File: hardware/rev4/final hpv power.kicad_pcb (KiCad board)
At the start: 2 copper layers, 69.5 x 54 mm, 27 parts, among them J1 Conn_02x03_Odd_Even, J2 Conn_01x04_Pin, Q1 PNP, U1 ESP32-S3-MINI-1, U2 MCP1825S, U3 HX711

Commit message: fixed up things for justin to look
fixed up things for justin to look
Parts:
- removed J1: Conn_02x03_Odd_Even, Connector_IDC:IDC-Header_2x03_P2.54mm_Vertical
- added J3: USB_C_Receptacle_USB2.0_14P, Connector_USB:USB_C_Receptacle_GCT_USB4110, F.Cu at (105.9, 102.3)
- added R7: 5.1k, Resistor_SMD:R_0805_2012Metric, F.Cu at (113.8, 99.1)
- added R8: 5.1k, Resistor_SMD:R_0805_2012Metric, F.Cu at (113.4, 106.0)
- C1, C10, C11, C12, C2, C3, C4, C5, C6, C7, C8, C9: footprint Capacitor_SMD:C_0603_1608Metric -> Capacitor_SMD:C_0805_2012Metric
- D1, D2: footprint LED_SMD:LED_0603_1608Metric -> LED_SMD:LED_0805_2012Metric
- R1, R2, R3, R4, R5, R6: footprint Resistor_SMD:R_0603_1608Metric -> Resistor_SMD:R_0805_2012Metric
- moved C3 6.66 mm to (130.6, 114.8)
- moved C2 6.61 mm to (127.5, 114.8)
- moved C5 6.53 mm to (121.2, 107.3)
- moved C7 6.53 mm to (121.2, 110.8)
- moved U2 6.53 mm to (127.8, 109.3)
- moved C1 6.50 mm to (124.4, 114.9)
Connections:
- net BATT renamed VBUS
- U1 pad 23: unconnected-(U1-USB_D--Pad23) -> /D-
- U1 pad 24: unconnected-(U1-USB_D+-Pad24) -> /D+
- U1 pad 39: /TX -> unconnected-(U1-TXD0-Pad39)
- U1 pad 40: /RX -> unconnected-(U1-RXD0-Pad40)
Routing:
- net VBUS: track 2.78 -> 39.5 mm
- net /D+: track 0.00 -> 30.2 mm, vias 0 -> 2
- net /D-: track 0.00 -> 30.1 mm, vias 0 -> 2
- net GND: track 115.0 -> 130.4 mm, vias 37 -> 45
- net /TX: track 11.0 -> 0.00 mm
- net /RX: track 10.3 -> 0.00 mm
- net Net-(J3-CC1): track 0.00 -> 4.10 mm
- net Net-(J3-CC2): track 0.00 -> 3.73 mm
- net +3.3V: track 23.3 -> 26.9 mm

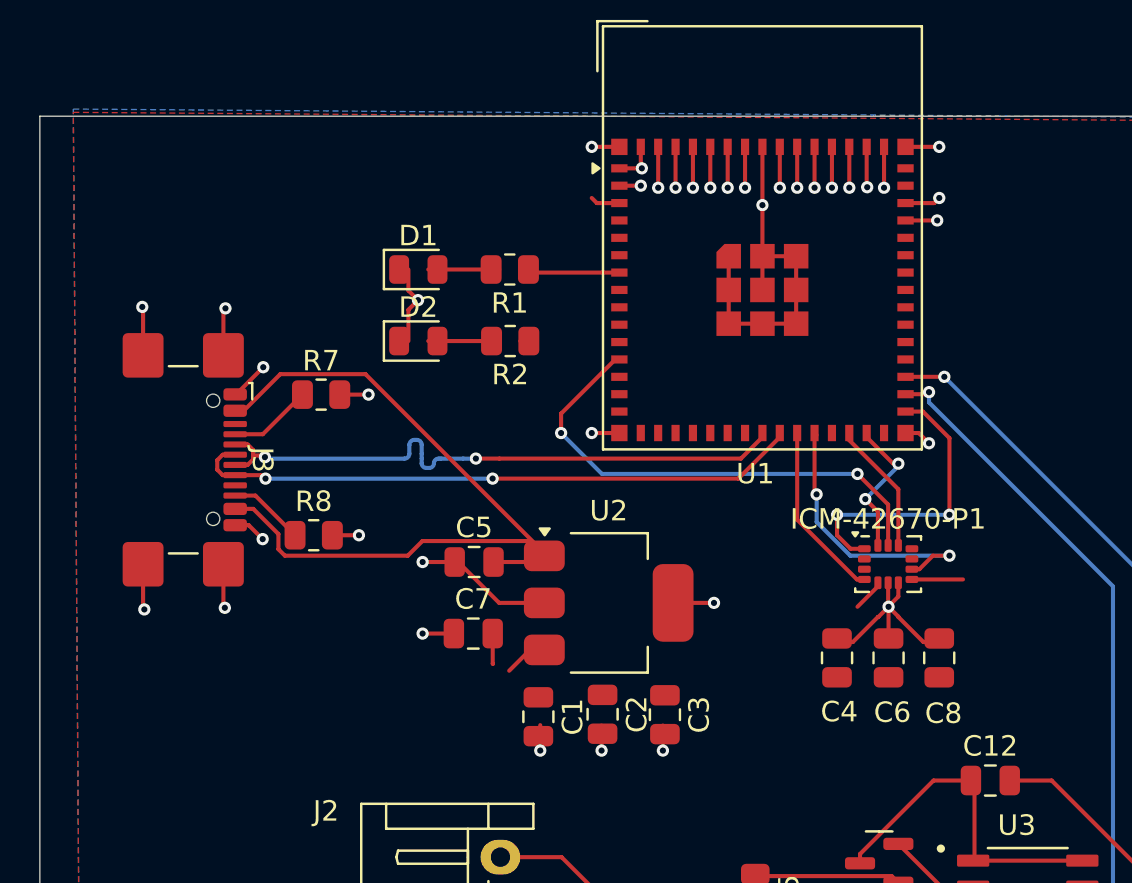
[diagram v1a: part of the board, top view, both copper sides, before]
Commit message: Update final hpv power.kicad_pcb
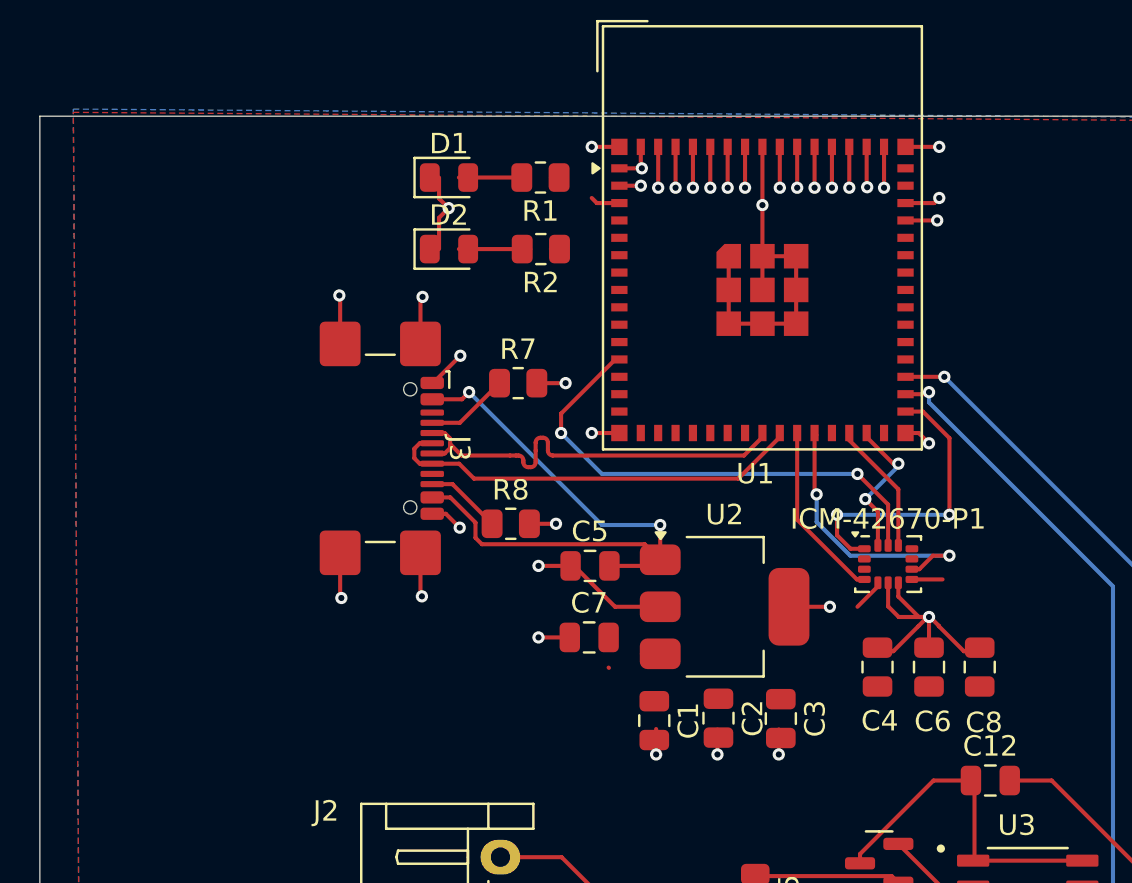
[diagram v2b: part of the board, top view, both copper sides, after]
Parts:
- moved R8 9.66 mm to (123.0, 105.4)
- moved J3 9.66 mm to (115.5, 101.8)
- moved R7 9.66 mm to (123.4, 98.6)
- moved C1 5.67 mm to (130.1, 115.1)
- moved C5 5.67 mm to (126.9, 107.5)
- moved C7 5.67 mm to (126.9, 111.0)
- moved U2 5.67 mm to (133.5, 109.5)
- moved C2 5.67 mm to (133.2, 115.0)
- moved C3 5.67 mm to (136.2, 115.0)
- moved D1 4.74 mm to (120.0, 88.5)
- moved D2 4.74 mm to (120.0, 92.0)
- moved R1 4.74 mm to (124.5, 88.5)
- moved R2 4.74 mm to (124.5, 92.0)
- moved C4 2.03 mm to (141.0, 112.5)
- moved C6 2.03 mm to (143.5, 112.5)
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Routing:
- net /D-: track 30.1 -> 20.7 mm, vias 2 -> 0
- net /D+: track 30.2 -> 20.8 mm, vias 2 -> 0
- net VBUS: track 39.5 -> 31.9 mm, vias 0 -> 2
- net /LED: track 4.91 -> 0.71 mm
- net +3.3V: track 26.9 -> 23.0 mm
- net GND: track 130.4 -> 133.5 mm

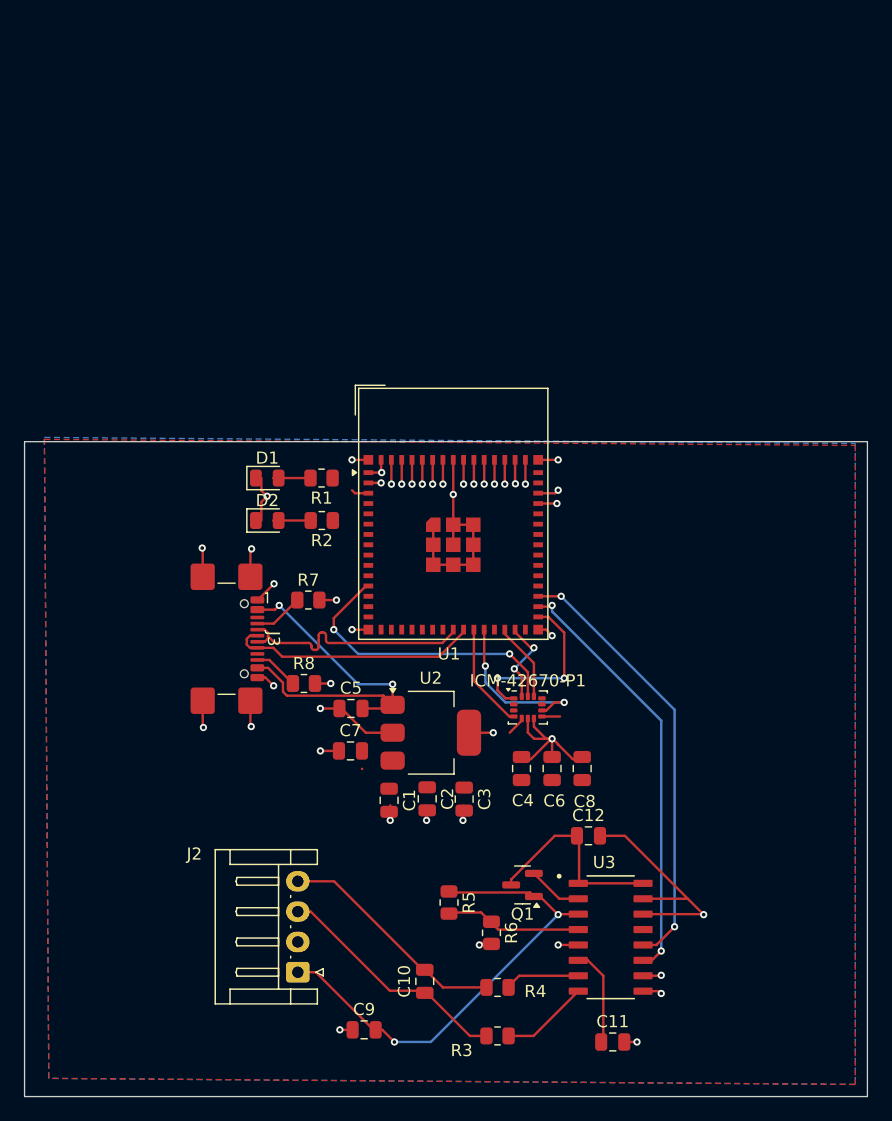
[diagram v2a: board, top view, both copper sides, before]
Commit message: Updated PCB and schematic for esp32 s3 wroom
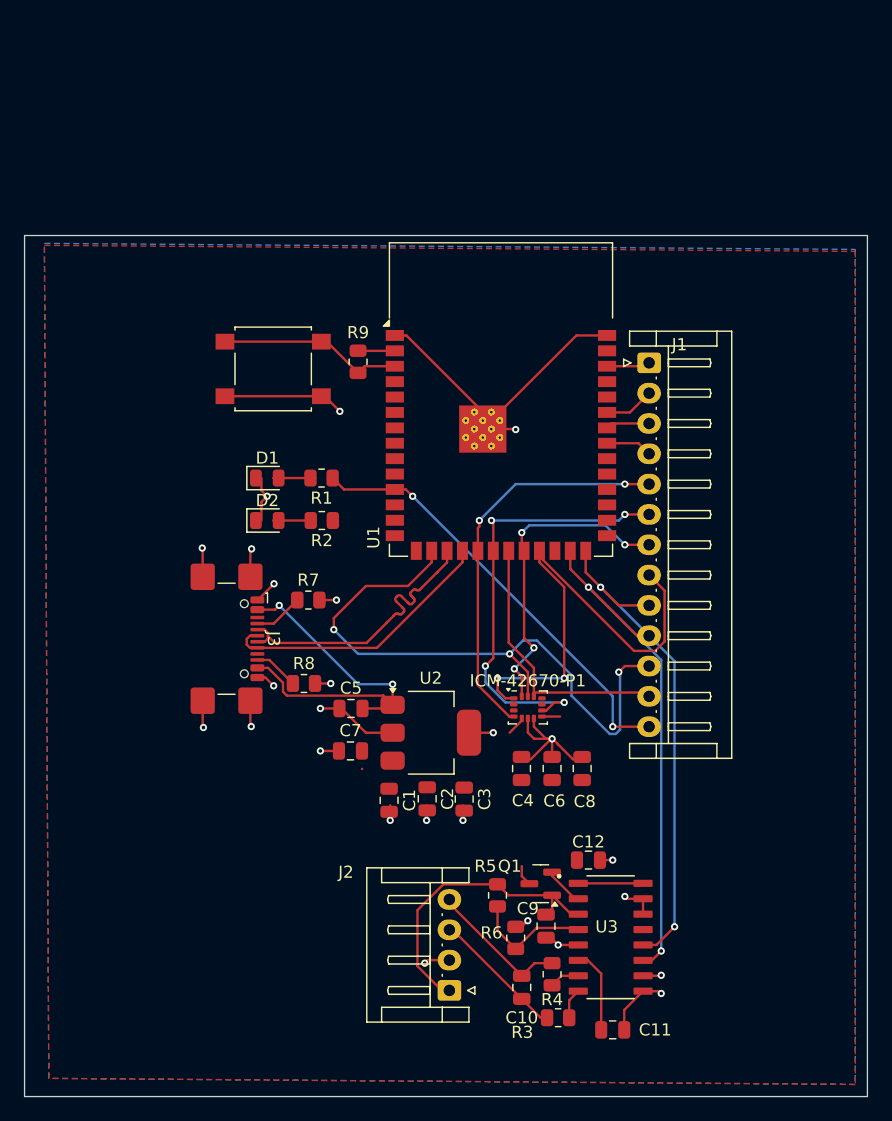
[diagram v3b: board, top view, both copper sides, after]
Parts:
- added J1: Conn_01x13_Pin, Connector_JST:JST_EH_S13B-EH_1x13_P2.50mm_Horizontal, F.Cu at (151.5, 79.0)
- added R9: 5.1k, Resistor_SMD:R_0805_2012Metric, F.Cu at (127.5, 78.9)
- added SW2: SW_SPST, Button_Switch_SMD:SW_SPST_B3S-1000, F.Cu at (120.5, 79.5)
- U1: value ESP32-S3-MINI-1 -> ESP32-S3-WROOM-1; footprint RF_Module:ESP32-S2-MINI-1 -> RF_Module:ESP32-S3-WROOM-1
- moved C9 17.3 mm to (143.0, 125.5), turned to 90 degrees
- moved J2 12.6 mm to (135.0, 130.8)
- moved U1 10.2 mm to (139.3, 82.0)
- moved C10 8.02 mm to (141.0, 130.5)
- moved R3 5.22 mm to (144.0, 133.0)
- moved R4 4.63 mm to (143.5, 129.4), turned to 90 degrees
- moved R5 4.04 mm to (139.0, 122.9)
- moved R6 2.04 mm to (140.5, 126.4)
- moved C12 2.00 mm to (146.5, 120.0)
- moved Q1 1.50 mm to (142.6, 122.0)
- moved C11 1.00 mm to (148.5, 134.0)
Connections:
- R6 pad 1: Net-(U3-VFB) -> GND
- R6 pad 2: GND -> Net-(U3-VFB)
- U1 pad 11: unconnected-(U1-IO7-Pad11) -> /LED
- U1 pad 12: /SCLK -> unconnected-(U1-IO8-Pad12)
- U1 pad 16: unconnected-(U1-IO12-Pad16) -> /SCLK
- U1 pad 17: unconnected-(U1-IO13-Pad17) -> /D-
- U1 pad 18: unconnected-(U1-IO14-Pad18) -> /D+
- U1 pad 19: unconnected-(U1-IO15-Pad19) -> /INT1 Gyro
- U1 pad 2: GND -> +3.3V
- U1 pad 20: unconnected-(U1-IO16-Pad20) -> /INT2 Gyro
- U1 pad 21: unconnected-(U1-IO17-Pad21) -> /CS Gyro
- U1 pad 22: unconnected-(U1-IO18-Pad22) -> /MOSI
- U1 pad 23: /D- -> /MISO
- U1 pad 24: /D+ -> unconnected-(U1-IO47-Pad24)
- U1 pad 25: /INT1 Gyro -> /HX711 PDSCK
- U1 pad 26: /INT2 Gyro -> /HX711 DOUT
- U1 pad 28: /CS Gyro -> unconnected-(U1-IO35-Pad28)
- U1 pad 29: /MOSI -> unconnected-(U1-IO36-Pad29)
- U1 pad 3: +3.3V -> Net-(SW2-A)
- U1 pad 31: /MISO -> unconnected-(U1-IO38-Pad31)
- U1 pad 32: /HX711 PDSCK -> unconnected-(U1-IO39-Pad32)
- U1 pad 33: /HX711 DOUT -> /GPIO12
- U1 pad 34: unconnected-(U1-IO38-Pad34) -> /GPIO11
- U1 pad 35: unconnected-(U1-IO39-Pad35) -> /GPIO10
- U1 pad 38: unconnected-(U1-IO42-Pad38) -> /GPIO9
- U1 pad 40: unconnected-(U1-RXD0-Pad40) -> GND
- U1 pad 41: unconnected-(U1-IO45-Pad41) -> GND
- U1 pad 7: /LED -> unconnected-(U1-IO7-Pad7)
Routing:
- net /LED: track 0.71 -> 36.8 mm, vias 0 -> 2
- net GND: track 133.5 -> 101.9 mm, vias 45 -> 25
- net /SCLK: track 24.3 -> 52.7 mm, vias 2 -> 3
- net /MISO: track 14.6 -> 39.8 mm
- net /INT1 Gyro: track 8.74 -> 32.9 mm, vias 0 -> 2
- net /INT2 Gyro: track 14.0 -> 36.5 mm, vias 2 -> 4
- net /MOSI: track 7.21 -> 26.2 mm, vias 2 -> 4
- net /CS Gyro: track 6.49 -> 22.8 mm
- net Net-(SW2-A): track 0.00 -> 15.3 mm
- net Net-(J2-Pin_1): track 39.6 -> 25.1 mm, vias 2 -> 0
- net /HX711 PDSCK: track 35.2 -> 44.6 mm
- net Net-(J2-Pin_3): track 19.9 -> 11.1 mm
- net +3.3V: track 23.0 -> 14.9 mm
- net Net-(J2-Pin_4): track 19.3 -> 11.7 mm
- net /HX711 DOUT: track 36.2 -> 41.9 mm
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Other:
- board size 69.5 x 54 mm -> 69.5 x 71 mm

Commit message: Rewired the HX711 on pcb and shrunk pcb size
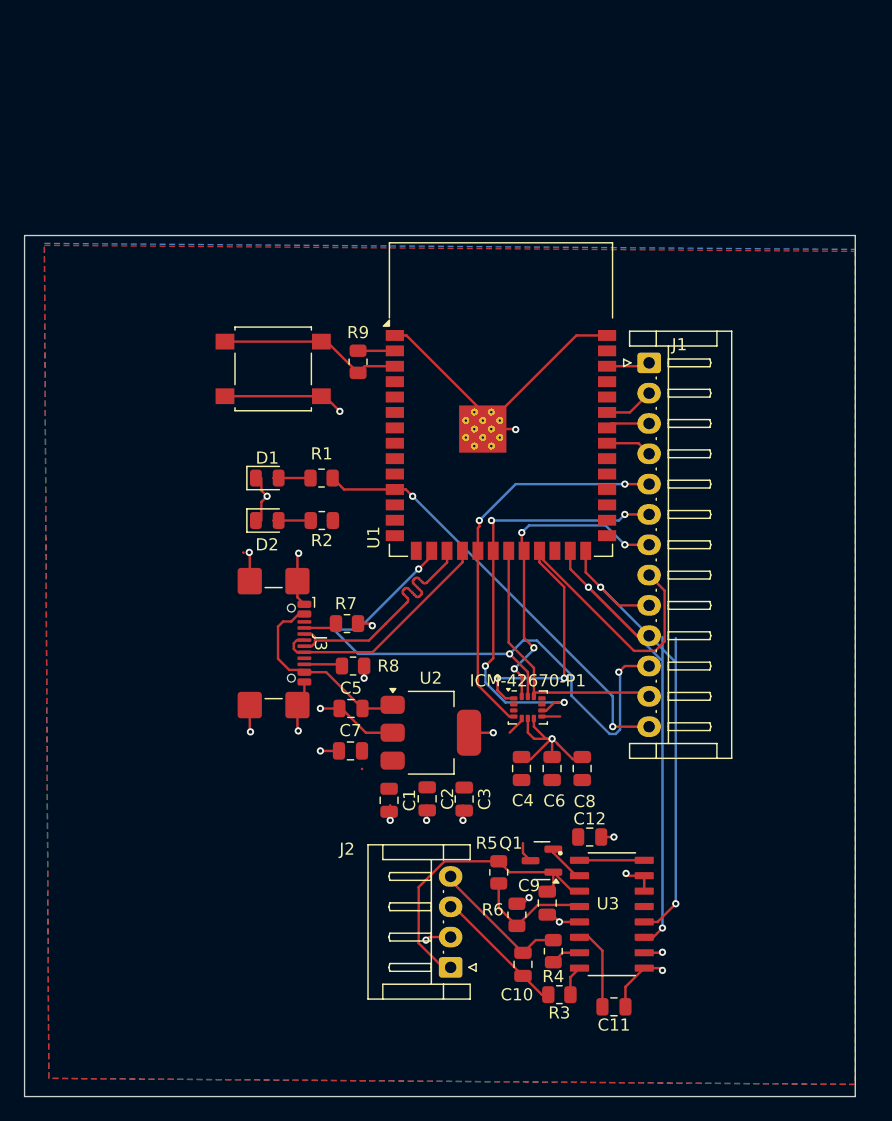
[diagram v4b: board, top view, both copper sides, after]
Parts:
- moved R8 4.30 mm to (127.1, 104.0)
- moved J3 3.90 mm to (119.4, 102.1)
- moved R7 3.73 mm to (126.6, 100.5)
- moved C10 1.90 mm to (141.1, 128.6)
- moved C11 1.90 mm to (148.6, 132.1)
- moved C12 1.90 mm to (146.6, 118.1)
- moved C9 1.90 mm to (143.1, 123.5)
- moved J2 1.90 mm to (135.1, 128.8)
- moved Q1 1.90 mm to (142.7, 120.0)
- moved R3 1.90 mm to (144.1, 131.1)
- moved R4 1.90 mm to (143.6, 127.5)
- moved R5 1.90 mm to (139.1, 121.0)
- moved R6 1.90 mm to (140.6, 124.5)
- moved U3 1.90 mm to (148.4, 124.5)
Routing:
- net VBUS: track 31.9 -> 16.8 mm, vias 2 -> 0
- net /D+: track 23.2 -> 19.5 mm
- net /D-: track 24.3 -> 20.6 mm
- net Net-(J3-CC1): track 4.10 -> 2.75 mm
- net Net-(J3-CC2): track 3.73 -> 3.16 mm
- net GND: track 101.9 -> 102.4 mm, vias 25 -> 23
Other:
- board size 69.5 x 71 mm -> 68.5 x 71 mm

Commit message: Fixing up PCB
added pull up resistor, replaced esp footprint, added header
made are a lot smaller
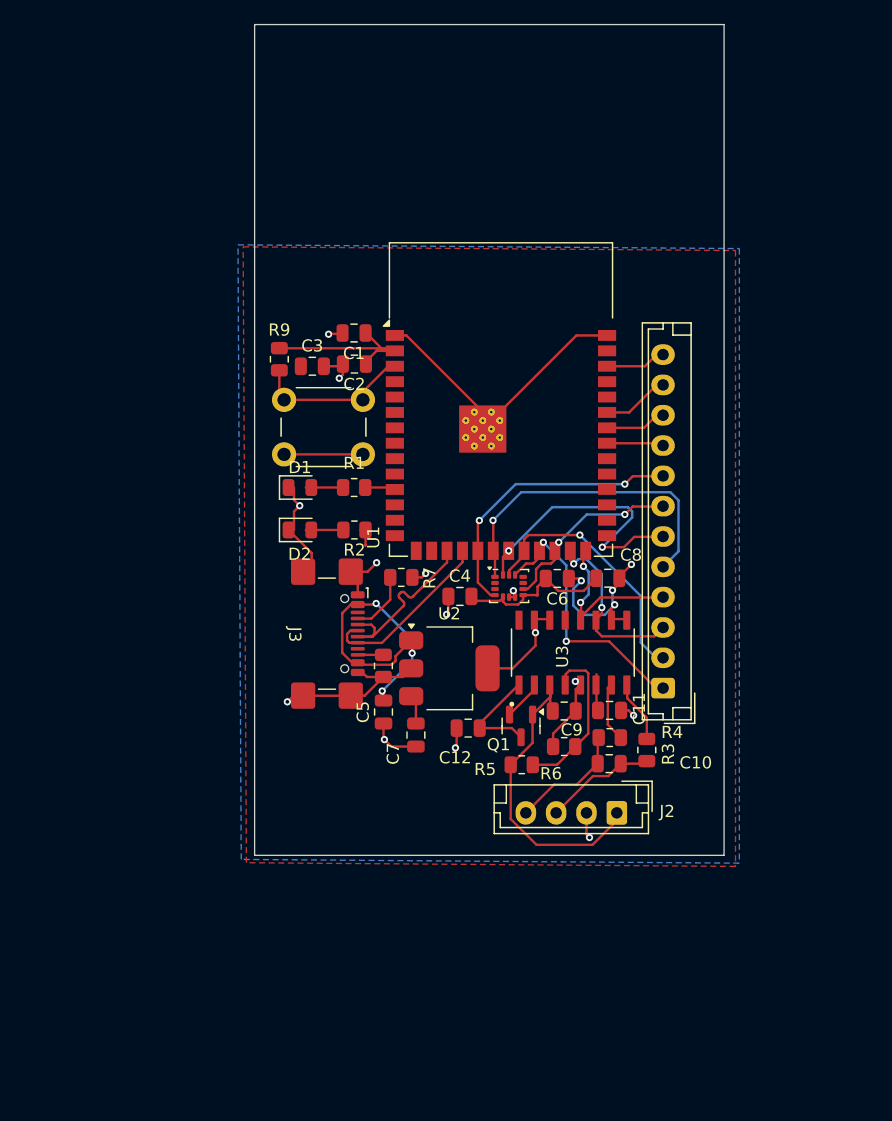
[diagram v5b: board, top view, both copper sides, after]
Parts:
- J1: value Conn_01x13_Pin -> Conn_01x12; footprint Connector_JST:JST_EH_S13B-EH_1x13_P2.50mm_Horizontal -> Connector_JST:JST_EH_B12B-EH-A_1x12_P2.50mm_Vertical
- J2: footprint Connector_JST:JST_EH_S4B-EH_1x04_P2.50mm_Horizontal -> Connector_JST:JST_EH_B4B-EH-A_1x04_P2.50mm_Vertical
- SW2: footprint Button_Switch_SMD:SW_SPST_B3S-1000 -> Button_Switch_THT:SW_PUSH_6mm_H4.3mm
- moved C1 38.6 mm to (127.2, 76.5), turned to 180 degrees
- moved C3 37.8 mm to (123.7, 79.3), turned to 0 degrees
- moved C2 36.3 mm to (127.2, 79.1), turned to 180 degrees
- moved J1 26.8 mm to (152.7, 105.8), turned to 90 degrees
- moved C11 24.4 mm to (148.2, 107.7)
- moved U3 21.8 mm to (145.2, 102.9), turned to 90 degrees
- moved R3 21.4 mm to (151.3, 110.9), turned to 90 degrees
- moved J2 18.7 mm to (148.8, 116.1), turned to 180 degrees
- moved R4 18.2 mm to (148.3, 109.9), turned to 180 degrees
- moved C10 18.0 mm to (148.2, 112.0), turned to 180 degrees
- moved C9 15.9 mm to (144.5, 107.7), turned to 180 degrees
- moved C8 15.8 mm to (148.1, 96.8), turned to 180 degrees
- moved C6 15.7 mm to (143.9, 96.8), turned to 180 degrees
- moved C4 15.1 mm to (135.9, 98.3), turned to 0 degrees
- moved R6 14.4 mm to (144.5, 110.6), turned to 0 degrees
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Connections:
- J1 pad 1: /GPIO9 -> /CS Gyro
- J1 pad 10: /HX711 PDSCK -> /GPIO11
- J1 pad 11: /SCLK -> /GPIO10
- J1 pad 12: /CS Gyro -> /GPIO9
- J1 pad 2: /GPIO10 -> /SCLK
- J1 pad 3: /GPIO11 -> /HX711 PDSCK
- J1 pad 4: /GPIO12 -> /HX711 DOUT
- J1 pad 5: /INT1 Gyro -> /MISO
- J1 pad 6: /INT2 Gyro -> /MOSI
- J1 pad 7: /MOSI -> /INT2 Gyro
- J1 pad 8: /MISO -> /INT1 Gyro
- J1 pad 9: /HX711 DOUT -> /GPIO12
- U1 pad 16: /SCLK -> unconnected-(U1-IO46-Pad16)
- U1 pad 20: /INT2 Gyro -> /MISO
- U1 pad 21: /CS Gyro -> /MOSI
- U1 pad 22: /MOSI -> /SCLK
- U1 pad 23: /MISO -> /CS Gyro
- U1 pad 24: unconnected-(U1-IO47-Pad24) -> /INT2 Gyro
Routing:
- net /LED: track 36.8 -> 3.22 mm, vias 2 -> 0
- net /SCLK: track 52.3 -> 21.8 mm, vias 3 -> 1
- net /HX711 PDSCK: track 44.6 -> 15.7 mm
- net /HX711 DOUT: track 41.9 -> 13.2 mm
- net +3.3V: track 14.9 -> 40.8 mm
- net /INT2 Gyro: track 36.5 -> 15.8 mm, vias 4 -> 2
- net /INT1 Gyro: track 32.9 -> 23.2 mm
- net /MISO: track 39.8 -> 30.3 mm, vias 2 -> 1
- net VBUS: track 16.8 -> 24.9 mm, vias 0 -> 3
- net /D-: track 20.6 -> 14.2 mm
- net /D+: track 19.5 -> 14.3 mm
- net /MOSI: track 26.2 -> 22.1 mm, vias 4 -> 2
- net Net-(U3-VBG): track 6.98 -> 3.03 mm
- net Net-(U3-VFB): track 10.1 -> 13.5 mm
- net Net-(U3-INA+): track 2.50 -> 5.21 mm
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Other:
- board size 68.5 x 71 mm -> 38.7 x 68.5 mm
